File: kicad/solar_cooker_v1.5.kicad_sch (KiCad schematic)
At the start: 20 parts, among them J1 Pt100, J4 Pt100, J6 GPS, J7 Pt100, J8 display, U2 microSD, U3 clock_module, U3 pyranometer, U5 anemometer, U6 BME680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

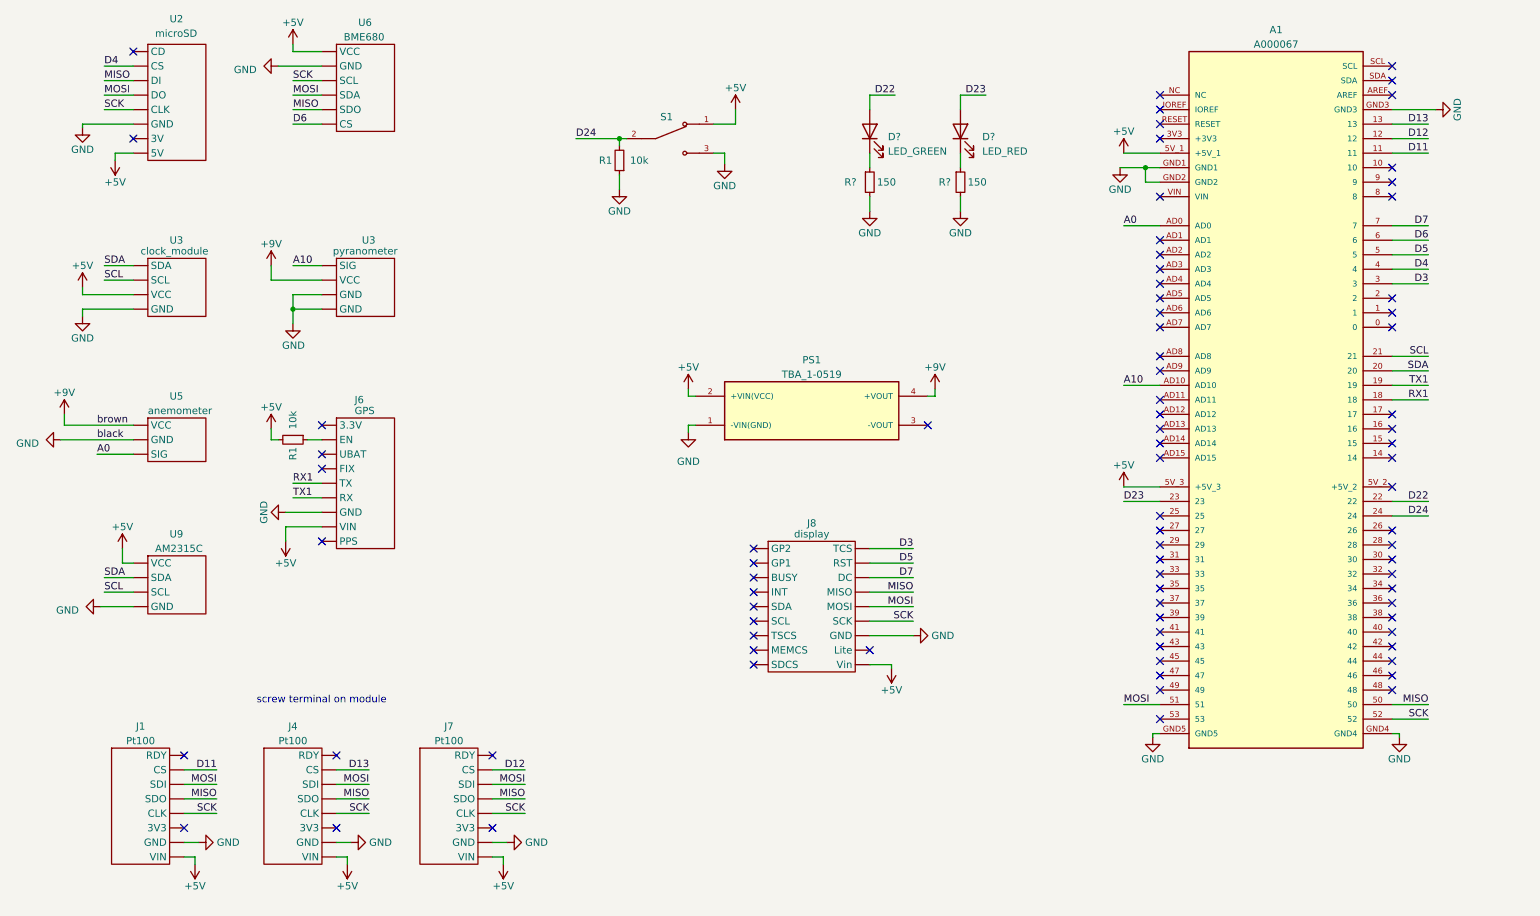
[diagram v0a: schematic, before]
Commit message: fixed GPS and clock module in kicad
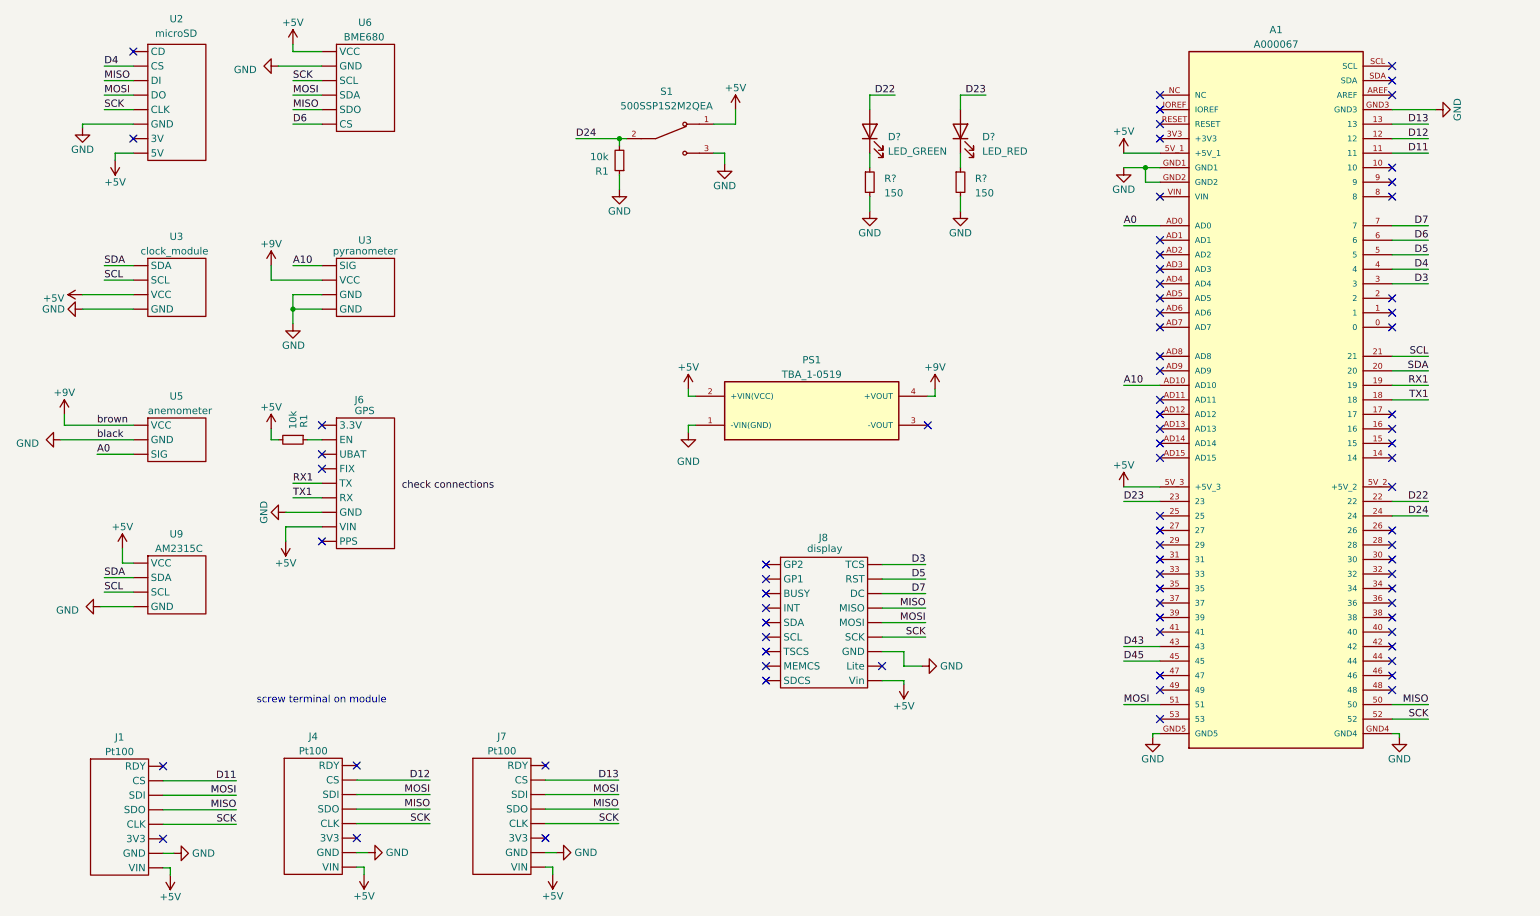
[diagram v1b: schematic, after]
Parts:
- J1, J4, J7: footprint custom_components:Pt100 -> custom_components:PT100
- PS1: footprint CONV_TBA_1-0519 -> dcdc convertor:CONV_TBA_1-0519
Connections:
- net D12: now also J4.2 (CS); no longer J7.2 (CS)
- net D13: now also J7.2 (CS); no longer J4.2 (CS)
- net RX1: now also A1.19; no longer A1.18
- net TX1: now also A1.18; no longer A1.19
- net D43: now reaches A1.43
- net D45: now reaches A1.45
- no-connect marks 82 -> 80

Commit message: footprints update
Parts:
- PS1: footprint dcdc convertor:CONV_TBA_1-0519 -> CONV_TBA_1-0519
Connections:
- net +5V: now also J1.1 (VIN), J4.1 (VIN), J7.1 (VIN), U2.1 (5V), U3.1 (VIN); no longer J1.8 (VIN), J4.8 (VIN), J7.8 (VIN), U2.8 (5V), U3.3 (VCC)
- net D11: now also J1.7 (CS); no longer J1.2 (CS)
- net D12: now also J4.7 (CS); no longer J4.2 (CS)
- net D13: now also J7.7 (CS); no longer J7.2 (CS)
- net D4: now also U2.7 (CS); no longer U2.2 (CS)
- net D6: now also U6.7 (CS); no longer U6.6 (CS)
- net GND: now also J1.2 (GND), J4.2 (GND), J7.2 (GND), U2.3 (GND), U3.2 (GND), U6.3 (GND); no longer J1.7 (GND), J4.7 (GND), J7.7 (GND), U2.6 (GND), U3.4 (GND), U6.2 (GND)
- net MISO: now also J1.5 (SDO), J4.5 (SDO), J7.5 (SDO), U2.6 (DI); no longer J1.4 (SDO), J4.4 (SDO), J7.4 (SDO), U2.3 (DI)
- net MOSI: now also J1.6 (SDI), J4.6 (SDI), J7.6 (SDI), U2.5 (DO), U6.6 (SDI); no longer J1.3 (SDI), J4.3 (SDI), J7.3 (SDI), U2.4 (DO), U6.4 (SDA)
- net SCK: now also J1.4 (CLK), J4.4 (CLK), J7.4 (CLK), U2.4 (CLK), U6.4 (SCK); no longer J1.5 (CLK), J4.5 (CLK), J7.5 (CLK), U2.5 (CLK), U6.3 (SCL)
- net SCL: now also U3.3 (SCL); no longer U3.2 (SCL)
- net SDA: now also U3.4 (SDA); no longer U3.1 (SDA)
- no-connect marks 80 -> 85
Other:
- moved on the sheet: U3

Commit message: all footprints ready
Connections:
- net +5V: now also J8.1 (Vin); no longer J8.9 (Vin)
- net D3: now also J8.9 (TCS); no longer J8.1 (TCS)
- net D5: now also J8.8 (RST); no longer J8.2 (RST)
- net D7: now also J8.7 (DC); no longer J8.3 (DC)
- net GND: now also J8.3 (GND); no longer J8.7 (GND)
- net MISO: now also J8.6 (MISO); no longer J8.4 (MISO)
- net SCK: now also J8.4 (SCK); no longer J8.6 (SCK)

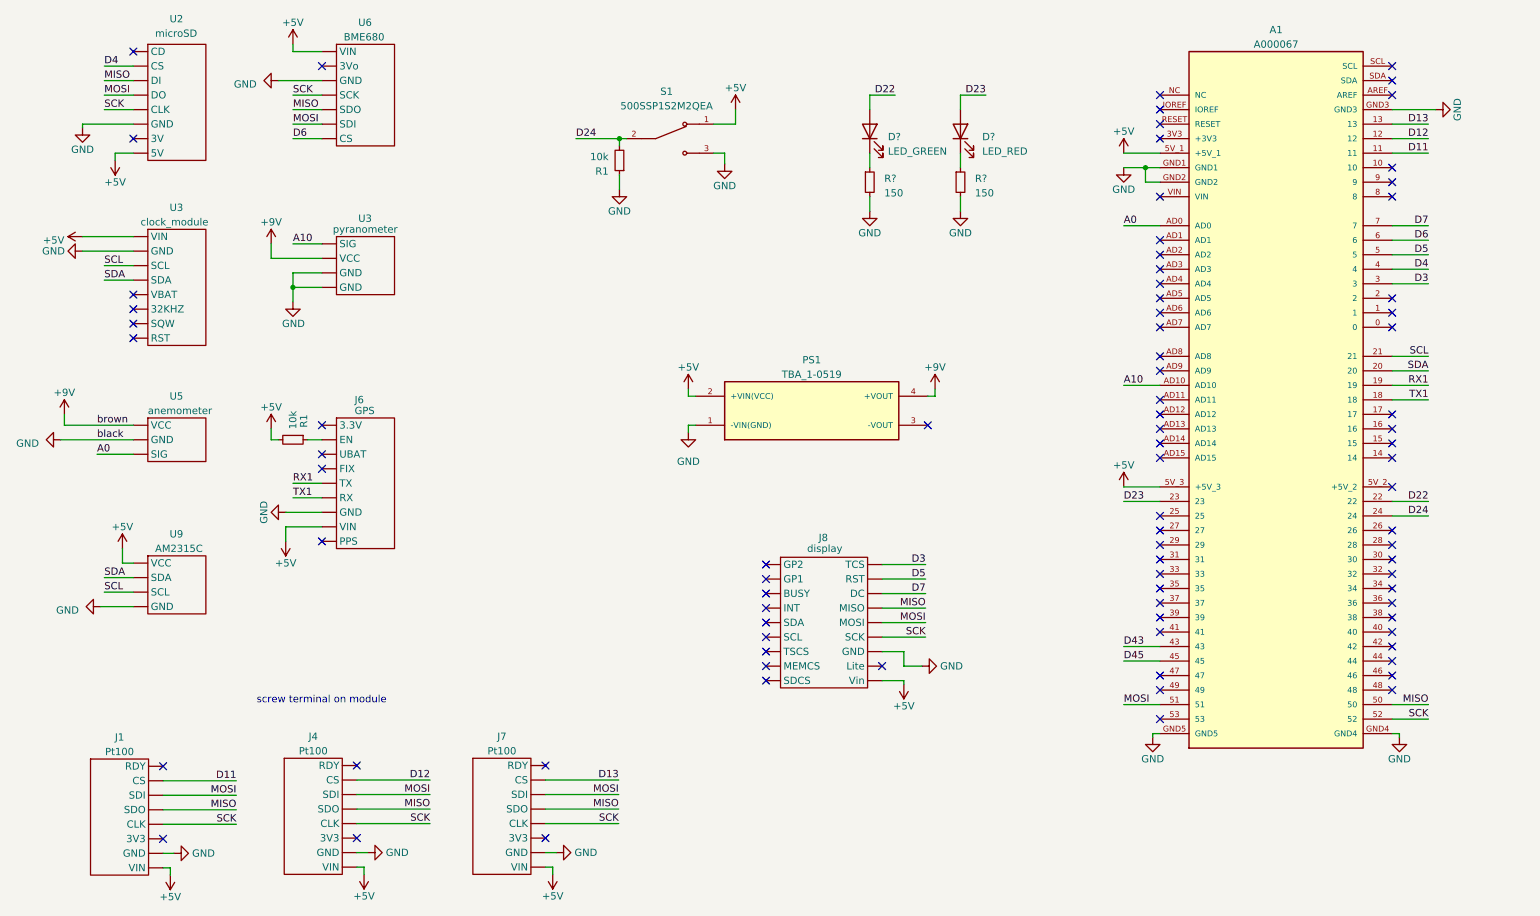
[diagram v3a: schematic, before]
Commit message: structure improvement kicad + added connectors
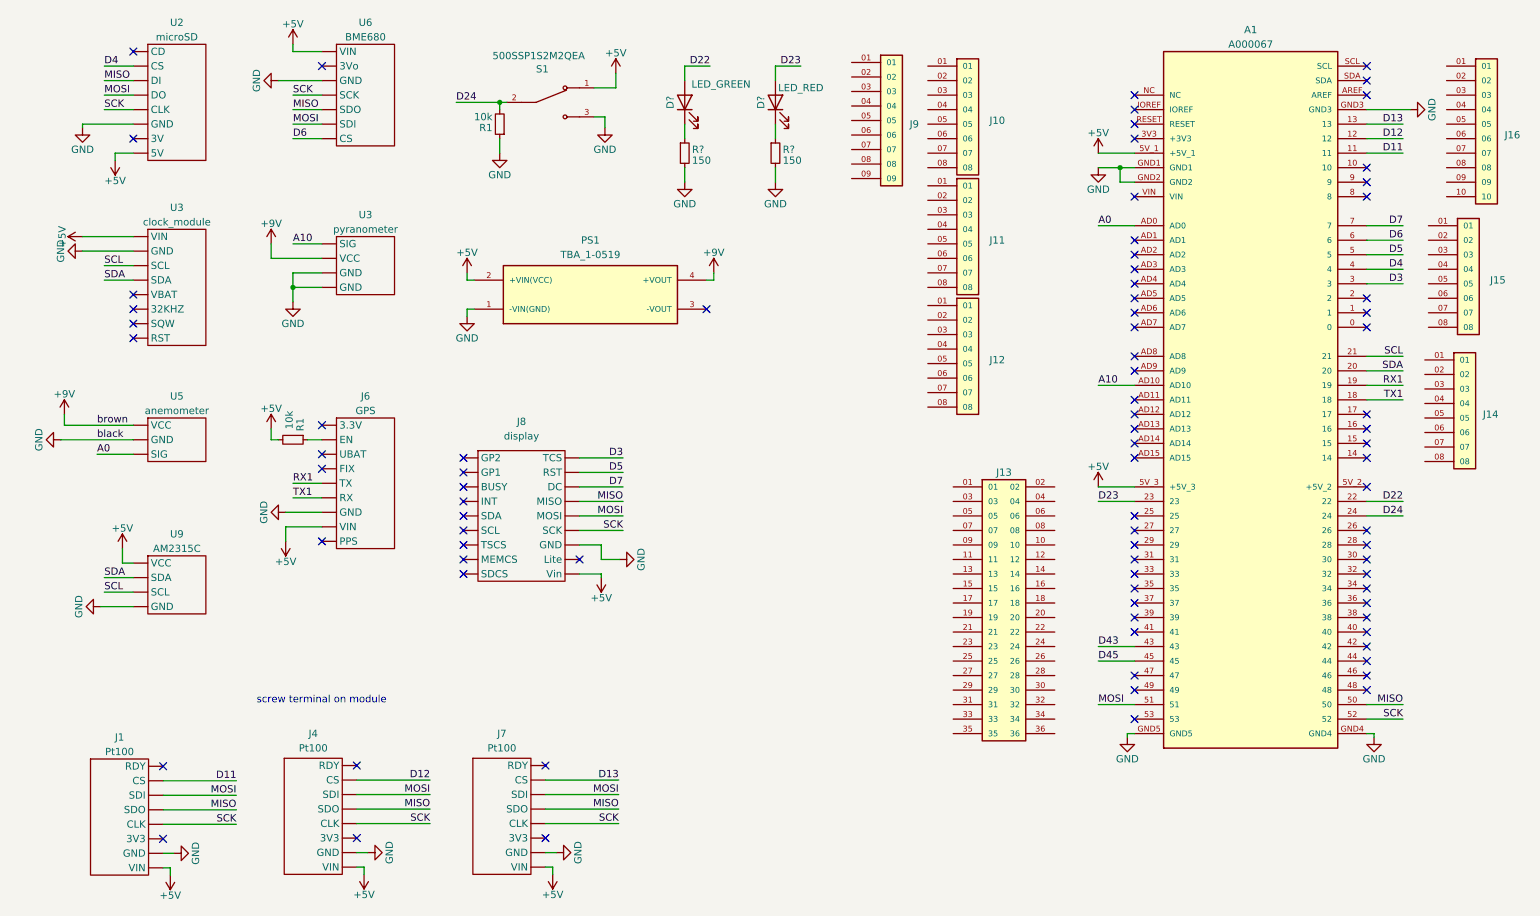
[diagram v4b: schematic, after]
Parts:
- added J10, J11, J12, J14, J15: SSQ-108-01-G-S, SSQ-108-01-G-S:SAMTEC_SSQ-108-01-G-S, symbol SSQ-108-01-G-S:SSQ-108-01-G-S
- added J13: SSQ-118-01-G-D, SAMTEC_SSQ-118-01-G-D, symbol SSQ-118-01-G-D:SSQ-118-01-G-D
- added J16: SSQ-110-01-G-S, SAMTEC_SSQ-110-01-G-S, symbol SSQ-110-01-G-S:SSQ-110-01-G-S
- added J9: SSQ-109-01-G-S, SAMTEC_SSQ-109-01-G-S, symbol SSQ-109-01-G-S:SSQ-109-01-G-S
- A1: symbol Arduino Mega:A000067 -> A000067:A000067; now left out of the parts list
- D?: footprint LED_SMD:LED_1206_3216Metric_Pad1.42x1.75mm_HandSolder -> (none); Component package type (none) -> 1206; MPN (none) -> QTLP650D2TR; Manufacturer (none) -> Everlight Electronics Co Ltd; SPN (none) -> 1080-1417-2-ND; Supplier (none) -> Digi-Key
- D?: footprint LED_SMD:LED_1206_3216Metric_Pad1.42x1.75mm_HandSolder -> (none); Component package type (none) -> 1206; MPN (none) -> 150120VS75000; Manufacturer (none) -> Würth Elektronik; SPN (none) -> 732-4993-1-ND; Supplier (none) -> Digi-Key
- J1, J4, J7: footprint custom_components:PT100 -> custom_components:Pt100; MPN (none) -> SSQ-108-01-G-S; Manufacturer (none) -> Samtec Inc.; SPN (none) -> SAM1180-08-ND; Supplier (none) -> Digi-Key
- J6: footprint custom_components:GPS -> (none); MPN (none) -> SSQ-109-01-G-S; Manufacturer (none) -> Samtec Inc.; SPN (none) -> SAM1180-09-ND; Supplier (none) -> Digi-Key
- J8: footprint custom_components:display -> (none); MPN (none) -> SSQ-109-01-G-S; Manufacturer (none) -> Samtec Inc.; SPN (none) -> SAM1180-09-ND; Supplier (none) -> Digi-Key
- PS1: symbol dcdc convertor:TBA_1-0519 -> TBA_1-0519:TBA_1-0519; MPN (none) -> TBA 1-0519; Manufacturer (none) -> Traco Power; SPN (none) -> 1951-3372-ND; Supplier (none) -> Digi-Key
- R1: footprint Resistor_SMD:R_1206_3216Metric -> (none); Component package type (none) -> R_1206; MPN (none) -> /; Manufacturer (none) -> /; SPN (none) -> GPR1206150R; Supplier (none) -> Eurocircuits
- R? (x2): footprint Resistor_SMD:R_1206_3216Metric_Pad1.30x1.75mm_HandSolder -> (none); Component package type (none) -> R_1206; MPN (none) -> /; Manufacturer (none) -> /; Productnumber CRGCQ1206F220R -> (none); SPN (none) -> GPR1206150R; Supplier (none) -> Eurocircuits
- S1: symbol switch:500SSP1S2M2QEA -> 500SSP1S2M2QEA:500SSP1S2M2QEA; MPN (none) -> 500SSP1S2M2QEA; Manufacturer (none) -> E-switch; SPN (none) -> EG5137-ND; Supplier (none) -> Digi-Key
- U2: footprint custom_components:microSD -> (none); MPN (none) -> SSQ-108-01-G-S; Manufacturer (none) -> Samtec Inc.; SPN (none) -> SAM1180-08-ND; Supplier (none) -> Digi-Key
- U3, U9: footprint custom_components:screw_terminal_4pin -> (none); MPN (none) -> 0395430004; Manufacturer (none) -> Molex; SPN (none) -> WM13967-ND; Supplier (none) -> Digi-Key
- U3: footprint custom_components:clockModule -> (none); MPN (none) -> SSQ-108-01-G-S; Manufacturer (none) -> Samtec Inc.; SPN (none) -> SAM1180-08-ND; Supplier (none) -> Digi-Key
- U5: footprint custom_components:screw_terminal_3pin -> (none); MPN (none) -> 0395430003; Manufacturer (none) -> Molex; SPN (none) -> WM9752-ND; Supplier (none) -> Digi-Key
- U6: footprint custom_components:BME680 -> (none); MPN (none) -> SAM1180-07-ND; Manufacturer (none) -> Digi-Key; SPN (none) -> SSQ-107-01-G-S; Supplier (none) -> Samtec Inc.
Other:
- moved on the sheet: A1, D?, J8, PS1, R1, R?, S1

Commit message: bom generation from schematic
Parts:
- A1: footprint ARDUINO_A000067 -> A000067:ARDUINO_A000067
- J9: MPN SSQ-108-01-G-S -> SSQ-109-01-G-S; SPN SAM1180-08-ND -> SAM1180-09-ND
- R1: SPN GPR1206150R -> GPR120610K
- U6: MPN SAM1180-07-ND -> SSQ-107-01-G-S; Manufacturer Digi-Key -> Samtec Inc.; SPN SSQ-107-01-G-S -> SAM1180-07-ND; Supplier Samtec Inc. -> Digi-Key
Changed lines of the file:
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@@
       (effects (font (size 1.27 1.27)) hide)
     )
-    (property "SPN" "GPR1206150R" (at 108.585 39.37 0)
+    (property "SPN" "GPR120610K" (at 108.585 39.37 0)
       (effects (font (size 1.27 1.27)) hide)
     )
@@
       (effects (font (size 1.27 1.27)) hide)
     )
-    (property "SPN" "GPR1206150R" (at 72.39 94.615 0)
+    (property "SPN" "GPR120610K" (at 72.39 94.615 0)
       (effects (font (size 1.27 1.27)) hide)
     )
@@
   )
   (symbol (lib_id "SSQ-109-01-G-S:SSQ-109-01-G-S") (at 175.26 38.735 0) (unit 1)
-    (in_bom yes) (on_board yes) (dnp no) (fields_autoplaced)
+    (in_bom yes) (on_board no) (dnp no) (fields_autoplaced)
     (property "Reference" "J9" (at 180.34 39.37 0)
       (effects (font (size 1.27 1.27)) (justify left))
@@
       (effects (font (size 1.27 1.27)) hide)
     )
-    (property "Description" "CONN RCPT 8POS 0.1 GOLD PCB" (at 175.26 38.735 0)
+    (property "Description" "CONN RCPT 9POS 0.1 GOLD PCB" (at 175.26 38.735 0)
       (effects (font (size 1.27 1.27)) hide)
     )
@@
       (effects (font (size 1.27 1.27)) hide)
     )
-    (property "MPN" "SSQ-108-01-G-S" (at 175.26 38.735 0)
+    (property "MPN" "SSQ-109-01-G-S" (at 175.26 38.735 0)
       (effects (font (size 1.27 1.27)) hide)
     )
@@
       (effects (font (size 1.27 1.27)) hide)
     )
-    (property "SPN" "SAM1180-08-ND" (at 175.26 38.735 0)
+    (property "SPN" "SAM1180-09-ND" (at 175.26 38.735 0)
       (effects (font (size 1.27 1.27)) hide)
     )
@@
       (effects (font (size 1.27 1.27)))
     )
-    (property "Footprint" "ARDUINO_A000067" (at 240.03 87.63 0)
+    (property "Footprint" "A000067:ARDUINO_A000067" (at 240.03 87.63 0)
       (effects (font (size 1.27 1.27)) (justify bottom) hide)
     )
@@
       (effects (font (size 1.27 1.27)) hide)
     )
-    (property "Manufacturer" "Digi-Key" (at 85.09 34.29 0)
-      (effects (font (size 1.27 1.27)) hide)
-    )
-    (property "MPN" "SAM1180-07-ND" (at 85.09 34.29 0)
-      (effects (font (size 1.27 1.27)) hide)
-    )
-    (property "Supplier" "Samtec Inc." (at 85.09 34.29 0)
-      (effects (font (size 1.27 1.27)) hide)
-    )
-    (property "SPN" "SSQ-107-01-G-S" (at 85.09 34.29 0)
-      (effects (font (size 1.27 1.27)) hide)
-    )
+    (property "Manufacturer" "Samtec Inc." (at 85.09 34.29 0)
+      (effects (font (size 1.27 1.27)) hide)
+    )
+    (property "MPN" "SSQ-107-01-G-S" (at 85.09 34.29 0)
+      (effects (font (size 1.27 1.27)) hide)
+    )
+    (property "Supplier" "Digi-Key" (at 85.09 34.29 0)
+      (effects (font (size 1.27 1.27)) hide)
+    )
+    (property "SPN" "SAM1180-07-ND" (at 85.09 34.29 0)
+      (effects (font (size 1.27 1.27)) hide)
+    )
